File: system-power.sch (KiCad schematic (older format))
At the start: 41 parts, among them IC1 TPS63031, J1 Conn_01x02, J2 Conn_01x02, U1 MCP73831T-2ACI/OT, U2 BQ25504

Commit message: Added notes for new design
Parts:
- added C?: C, symbol Device:C
- added D?: ca. 2.2V, symbol Device:D_Zener
- added R?: 150R, symbol Device:R
- added R? (x2): 5.49M, symbol Device:R
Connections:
- net EXT_VIN: now also D?.2 (A)
- net GND: now also C?.1, R?.1, R?.2
- net VBAT_OK: now also IC1.6 (EN)
- net VBUS: now also R?.1
- net at C6.1, IC1.5 (Vin), JP2.2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: now also R?.2
- net at C7.1, IC1.7 (PS/SYNC), IC1.8 (VinA): no longer IC1.6 (EN)
- net at JP1.1, U2.14 (VBAT): now also C?.2
- new net: D?.1 (K), R?.2
- new net VSTOR: R?.1
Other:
- note added: "Dieses C ist evtl. nicht optimal\nplatziert. Mit KO vor BQ, nach BQ\nund nach DCDC-Converter Messen\nund analysieren, wo Spannung\nzusammenfällt"
- note added: "Maximum R probieren \nund dann 1-2 Werte zurück\n"
- note added: "Settings for BQ25504:\n\nVBAT_OV: 4.147 V --------\nVBAT_UV: 2.998 V\nVBAT_OK: 3.086 V\nVBAT_OK_HYST: 4.095 V\nVREF_SAMP: 0.8 V"
- note added: "Spannungsteiler für Messung\nder Batterie-Spannung. \nStimmen R?"
- note removed: "Settings for BQ25504:\n\nVBAT_OV: 4.147 V\nVBAT_UV: 2.998 V\nVBAT_OK: 3.086 V\nVBAT_OK_HYST: 4.095 V\nVREF_SAMP: 0.8 V"
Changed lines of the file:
@@
 	8350 3750 8100 3750
 Wire Wire Line
-	8100 3750 8100 3850
-Wire Wire Line
-	8350 3850 8100 3850
-Connection ~ 8100 3850
-Wire Wire Line
-	8100 3850 8100 3950
-Wire Wire Line
 	8350 3950 8100 3950
-Connection ~ 8100 3950
 Wire Wire Line
 	8350 3650 7700 3650
@@
 	2850 1650 3600 1650
 Connection ~ 3600 1650
-Text Notes 1150 3100 0    50   Italic 0
+Text Notes 500  4000 0    50   Italic 0
 For optimum voltage regulation, \nplace the battery pack as close as \npossible to the device’s VBAT and VSS pins.
 Text Notes 9800 3450 0    50   ~ 0
@@
 Connection ~ 1800 4750
 Wire Wire Line
-	1800 4750 2250 4750
+	1800 4750 2200 4750
 Wire Wire Line
 	1800 5150 1800 5200
 Wire Wire Line
 	3200 3950 3150 3950
-Wire Wire Line
-	3150 3950 3150 2850
 Wire Wire Line
 	3150 2850 3800 2850
@@
 Connection ~ 2250 4750
 Wire Wire Line
-	2250 4750 2550 4750
+	2250 4750 2200 4750
 $Comp
 L Device:LED D3
@@
 $EndComp
 Text Notes 4750 6850 0    50   ~ 0
-Settings for BQ25504:\n\nVBAT_OV: 4.147 V\nVBAT_UV: 2.998 V\nVBAT_OK: 3.086 V\nVBAT_OK_HYST: 4.095 V\nVREF_SAMP: 0.8 V
+Settings for BQ25504:\n\nVBAT_OV: 4.147 V --------\nVBAT_UV: 2.998 V\nVBAT_OK: 3.086 V\nVBAT_OK_HYST: 4.095 V\nVREF_SAMP: 0.8 V
 $Comp
 L power:PWR_FLAG #FLG02
@@
 	3600 1650 4100 1650
 Wire Wire Line
-	5750 3650 7700 3650
-Wire Wire Line
 	4500 2300 4500 2850
 Wire Wire Line
@@
 Wire Wire Line
 	2950 2550 2950 2600
-Wire Wire Line
-	2950 2600 1850 2600
 Wire Wire Line
 	1850 1450 1850 2600
@@
 Wire Wire Line
 	3100 5600 3100 5700
+Wire Wire Line
+	2200 3350 2200 4750
+Connection ~ 2200 4750
+$Comp
+L Device:C C?
+U 1 1 5F9DF573
+P 3400 3150
+F 0 "C?" V 3148 3150 50  0000 C CNN
+F 1 "C" V 3239 3150 50  0000 C CNN
+F 2 "" H 3438 3000 50  0001 C CNN
+F 3 "~" H 3400 3150 50  0001 C CNN
+	1    3400 3150
+	0    1    1    0
+$EndComp
+Wire Wire Line
+	3150 3150 3250 3150
+Connection ~ 3150 3150
+Wire Wire Line
+	3150 3150 3150 2850
+$Comp
+L power:GND #PWR?
+U 1 1 5F9E9D86
+P 3700 3200
+F 0 "#PWR?" H 3700 2950 50  0001 C CNN
+F 1 "GND" H 3705 3027 50  0000 C CNN
+F 2 "" H 3700 3200 50  0001 C CNN
+F 3 "" H 3700 3200 50  0001 C CNN
+	1    3700 3200
+	1    0    0    -1
+$EndComp
+Wire Wire Line
+	3700 3200 3700 3150
+Wire Wire Line
+	3700 3150 3550 3150
+Wire Wire Line
+	3150 3150 3150 3950
+Wire Wire Line
+	2200 2600 2200 2700
+Wire Wire Line
+	1850 2600 2200 2600
+Connection ~ 2200 2600
+Wire Wire Line
+	2200 2600 2950 2600
+Wire Wire Line
+	2250 4750 2550 4750
+$Comp
+L Device:R R?
+U 1 1 5FA4E351
+P 2200 2850
+F 0 "R?" H 2270 2896 50  0000 L CNN
+F 1 "150R" H 2270 2805 50  0000 L CNN
+F 2 "" V 2130 2850 50  0001 C CNN
+F 3 "~" H 2200 2850 50  0001 C CNN
+	1    2200 2850
+	1    0    0    -1
+$EndComp
+Wire Wire Line
+	2200 3000 2200 3050
+$Comp
+L Device:D_Zener D?
+U 1 1 5FA540F4
+P 2200 3200
+F 0 "D?" V 2154 3279 50  0000 L CNN
+F 1 "ca. 2.2V" V 2245 3279 50  0000 L CNN
+F 2 "" H 2200 3200 50  0001 C CNN
+F 3 "~" H 2200 3200 50  0001 C CNN
+	1    2200 3200
+	0    1    1    0
+$EndComp
+Text Notes 1050 3100 0    50   Italic 0
+Maximum R probieren \nund dann 1-2 Werte zurück\n
+Text GLabel 7500 4050 0    50   Input ~ 0
+VBAT_OK
+Wire Wire Line
+	7350 4050 8000 4050
+Wire Wire Line
+	8000 4050 8000 3850
+Wire Wire Line
+	8350 3850 8000 3850
+Wire Wire Line
+	8100 3750 8100 3950
+Connection ~ 8100 3950
+Text GLabel 6750 2750 1    50   Output ~ 0
+VSTOR
+Wire Wire Line
+	5750 3650 6750 3650
+$Comp
+L Device:R R?
+U 1 1 5FAAB7C8
+P 6750 3400
+F 0 "R?" H 6820 3446 50  0000 L CNN
+F 1 "5.49M" H 6820 3355 50  0000 L CNN
+F 2 "" V 6680 3400 50  0001 C CNN
+F 3 "~" H 6750 3400 50  0001 C CNN
+	1    6750 3400
+	1    0    0    -1
+$EndComp
+$Comp
+L Device:R R?
+U 1 1 5FAAEB35
+P 6750 3000
+F 0 "R?" H 6820 3046 50  0000 L CNN
+F 1 "5.49M" H 6820 2955 50  0000 L CNN
+F 2 "" V 6680 3000 50  0001 C CNN
+F 3 "~" H 6750 3000 50  0001 C CNN
+	1    6750 3000
+	1    0    0    -1
+$EndComp
+Wire Wire Line
+	6750 3250 6750 3200
+Wire Wire Line
+	6750 2850 6750 2750
+Wire Wire Line
+	6750 3650 6750 3550
+Connection ~ 6750 3650
+Wire Wire Line
+	6750 3650 7700 3650
+$Comp
+L power:GND #PWR?
+U 1 1 5FACE2D9
+P 6500 3300
+F 0 "#PWR?" H 6500 3050 50  0001 C CNN
+F 1 "GND" H 6505 3127 50  0000 C CNN
+F 2 "" H 6500 3300 50  0001 C CNN
+F 3 "" H 6500 3300 50  0001 C CNN
+	1    6500 3300
+	1    0    0    -1
+$EndComp
+Wire Wire Line
+	6500 3300 6500 3200
+Wire Wire Line
+	6500 3200 6750 3200
+Connection ~ 6750 3200
+Wire Wire Line
+	6750 3200 6750 3150
+Text Notes 5550 3050 0    50   Italic 0
+Spannungsteiler für Messung\nder Batterie-Spannung. \nStimmen R?
+Text Notes 3750 3300 0    50   Italic 0
+Dieses C ist evtl. nicht optimal\nplatziert. Mit KO vor BQ, nach BQ\nund nach DCDC-Converter Messen\nund analysieren, wo Spannung\nzusammenfällt
 $EndSCHEMATC

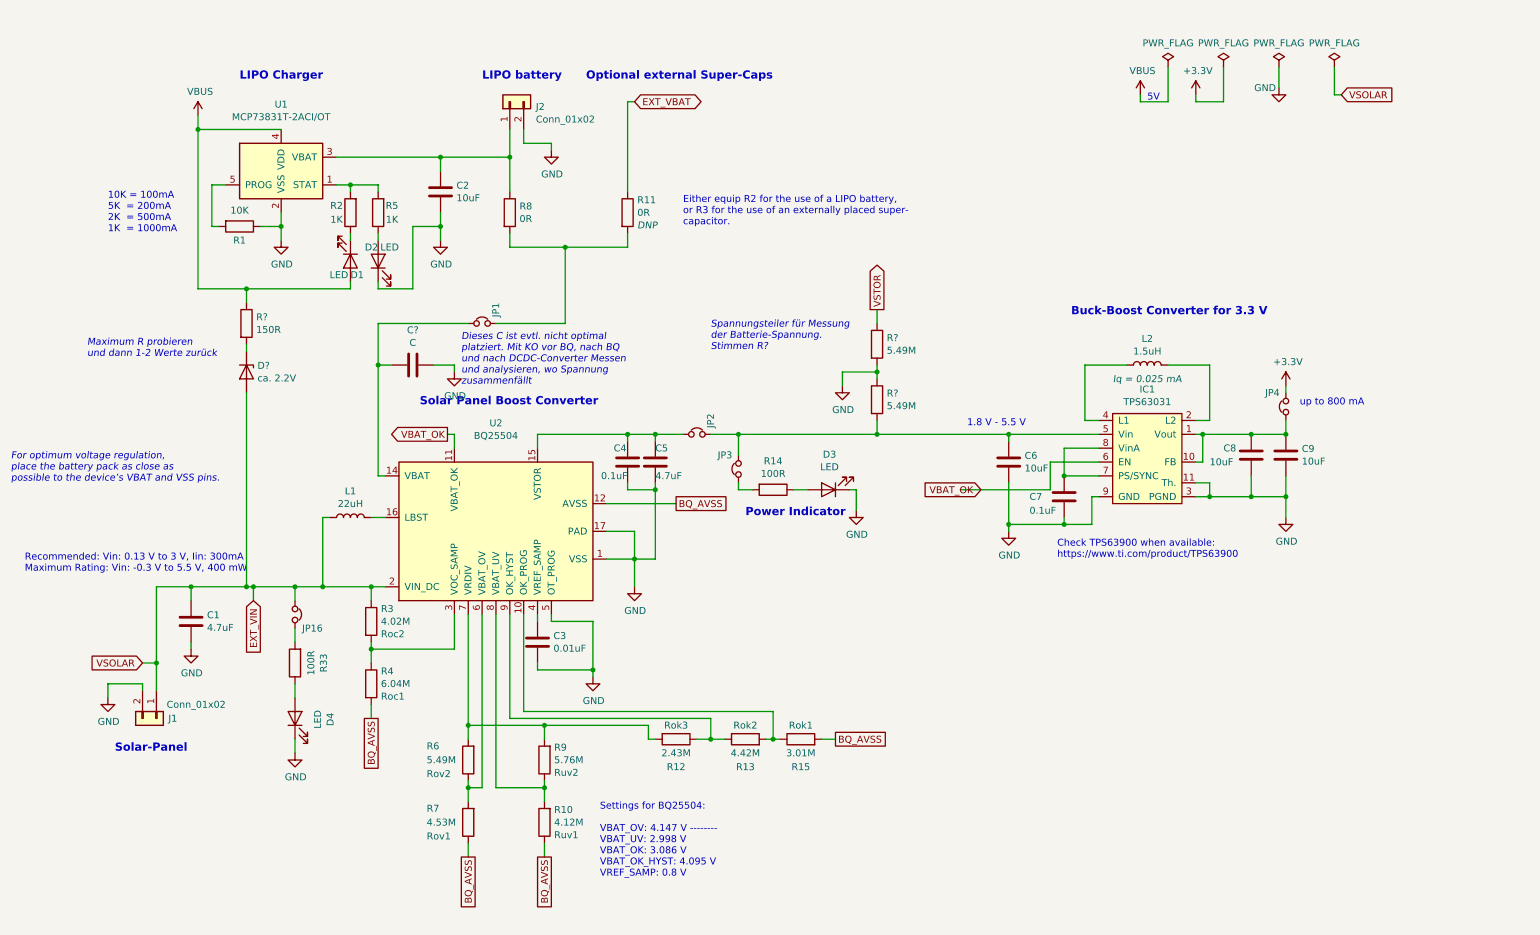
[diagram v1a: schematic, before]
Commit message: Fixed issue #2, #3, #4 and #5
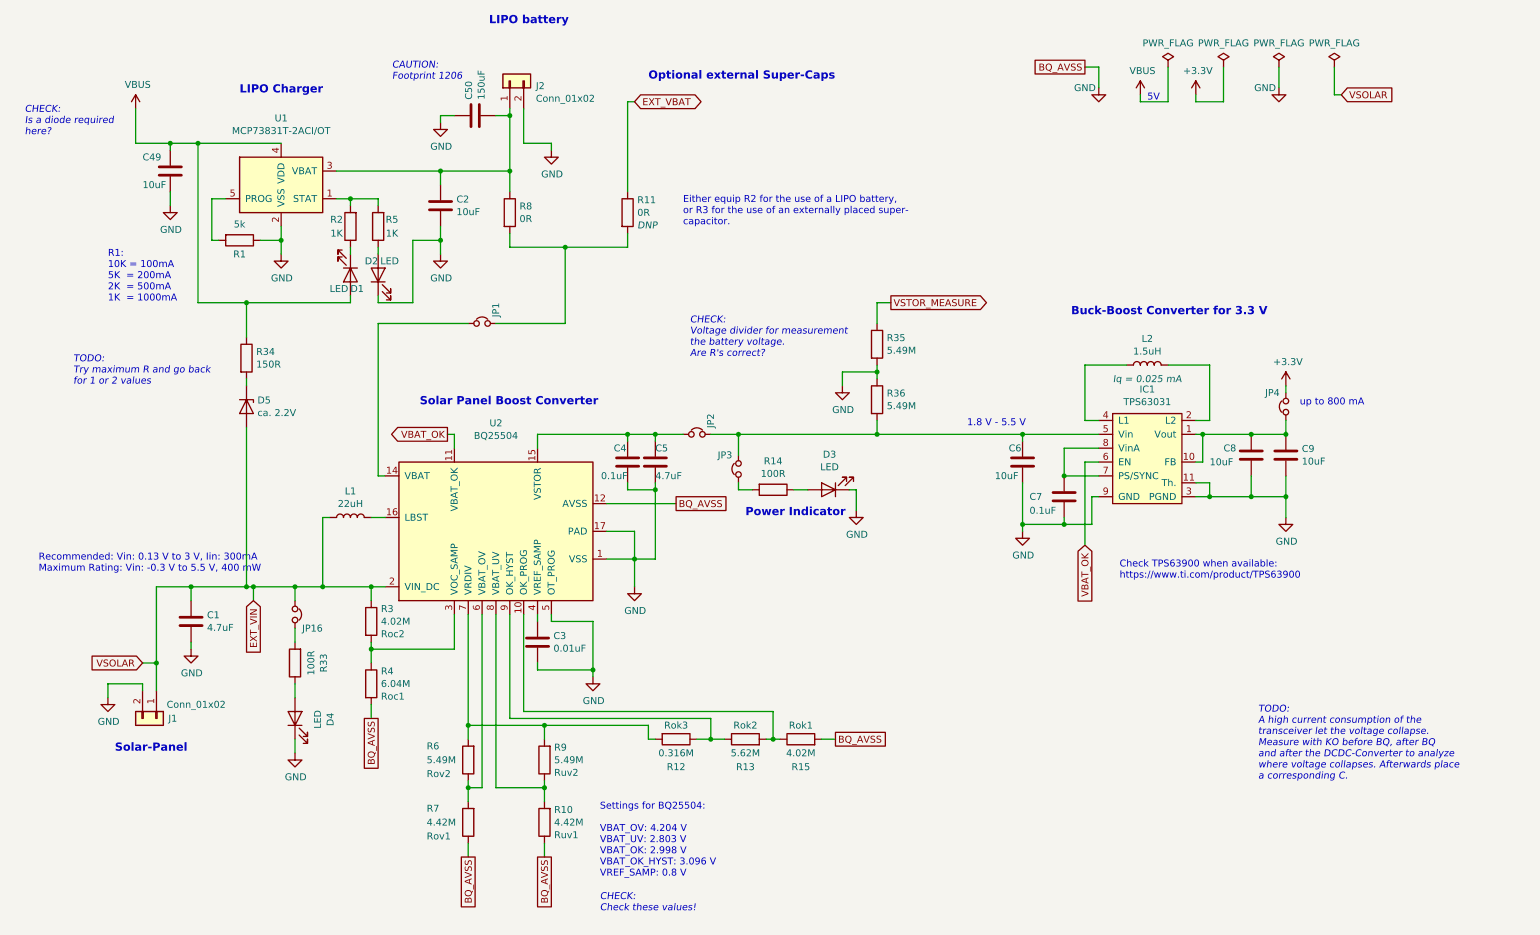
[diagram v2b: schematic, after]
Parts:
- removed C?: C, symbol Device:C
- added C49: 10uF, Capacitor_SMD:C_0402_1005Metric, symbol Device:C
- added C50: 150uF, Capacitor_SMD:C_0402_1005Metric, symbol Device:C
- R1: value 10K -> 5k
- R10: value 4.12M -> 4.42M
- R12: value 2.43M -> 0.316M
- R13: value 4.42M -> 5.62M
- R15: value 3.01M -> 4.02M
- R7: value 4.53M -> 4.42M
- R9: value 5.76M -> 5.49M
- gave numbers to parts that had none: 4
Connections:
- net BQ_AVSS is gone; now on net GND: R10.1, R15.2, R4.2, R7.1, U2.12 (AVSS)
- net GND: now also C49.2, C50.1
- net VBUS: now also C49.1
- net at C2.1, J2.1 (Pin_1), R8.1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: now also C50.2
- net VSTOR renamed VSTOR_MEASURE
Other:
- note added: "CAUTION:\nFootprint 1206"
- note added: "CHECK:\nCheck these values!"
- note added: "CHECK:\nIs a diode required \nhere?"
- note added: "CHECK:\nVoltage divider for measurement\nthe battery voltage. \nAre R's correct?"
- note added: "R1:\n10K = 100mA\n5K = 200mA\n2K = 500mA\n1K = 1000mA"
- note added: "Settings for BQ25504:\n\nVBAT_OV: 4.204 V\nVBAT_UV: 2.803 V\nVBAT_OK: 2.998 V\nVBAT_OK_HYST: 3.096 V\nVREF_SAMP: 0.8 V"
- note added: "TODO:\nA high current consumption of the\ntransceiver let the voltage collapse.\nMeasure with KO before BQ, after BQ\nand after the DCDC-Converter to analyze \nwhere voltage collapses. Afterwards place\na corresponding C."
- note added: "TODO:\nTry maximum R and go back\nfor 1 or 2 values"
- note removed: "10K = 100mA\n5K = 200mA\n2K = 500mA\n1K = 1000mA"
- note removed: "Dieses C ist evtl. nicht optimal\nplatziert. Mit KO vor BQ, nach BQ\nund nach DCDC-Converter Messen\nund analysieren, wo Spannung\nzusammenfällt"
- note removed: "For optimum voltage regulation, \nplace the battery pack as close as \npossible to the device’s VBAT and VSS pins."
- note removed: "Maximum R probieren \nund dann 1-2 Werte zurück\n"
- note removed: "Settings for BQ25504:\n\nVBAT_OV: 4.147 V --------\nVBAT_UV: 2.998 V\nVBAT_OK: 3.086 V\nVBAT_OK_HYST: 4.095 V\nVREF_SAMP: 0.8 V"
- note removed: "Spannungsteiler für Messung\nder Batterie-Spannung. \nStimmen R?"
- moved on the sheet: C2, C6, D1, D2, D5, J2, R1, R2, R34, R5, U1

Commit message: Removed unnecessary leds from system-power to save power
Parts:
- removed D3, D4: LED, LED_SMD:LED_0603_1608Metric, symbol Device:LED
- removed JP16, JP3: Jumper_NC_Small, Connector_PinHeader_2.54mm:PinHeader_1x02_P2.54mm_Vertical, symbol Device:Jumper_NC_Small
- removed R14, R33: 100R, Resistor_SMD:R_0402_1005Metric, symbol Device:R
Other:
- note removed: "Power Indicator"

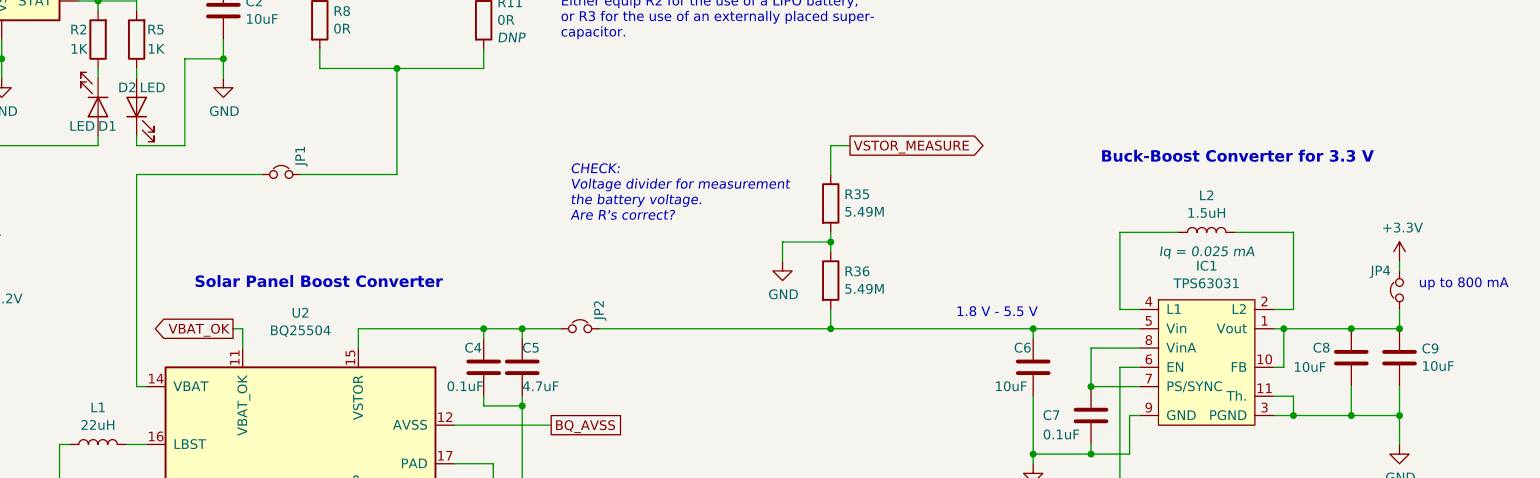
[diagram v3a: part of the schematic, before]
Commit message: Removed jumpers from system-power
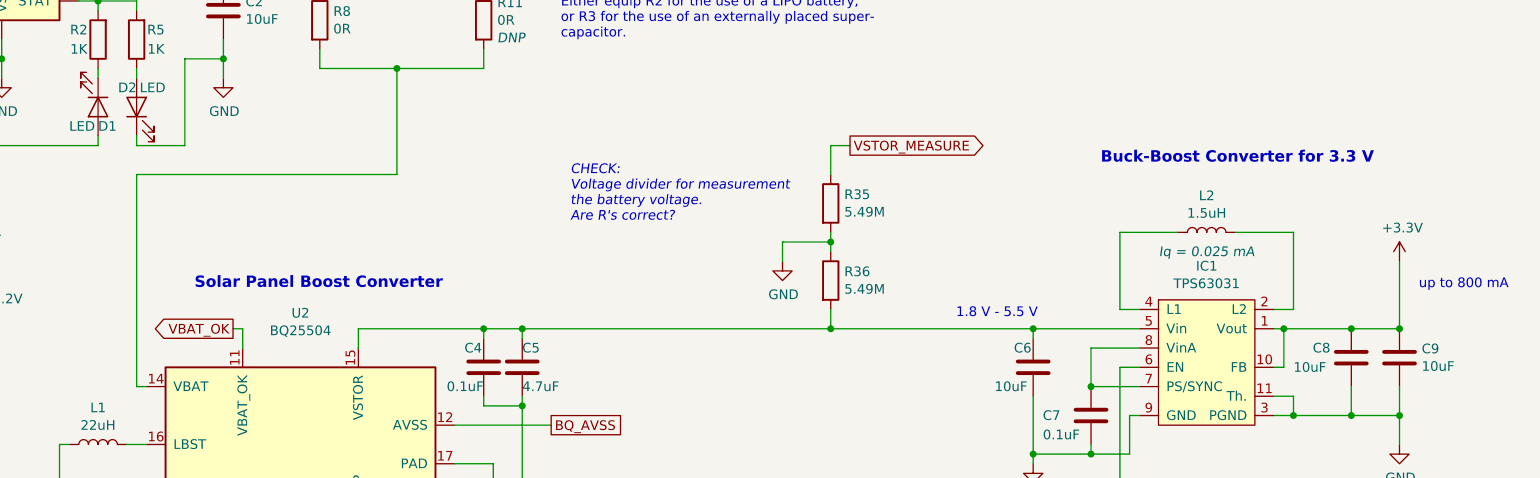
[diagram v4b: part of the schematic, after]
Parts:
- removed JP1, JP2, JP4: Jumper_NC_Small, Connector_PinHeader_2.54mm:PinHeader_1x02_P2.54mm_Vertical, symbol Device:Jumper_NC_Small
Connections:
- net +3V3: now also C8.1, C9.1, IC1.1 (Vout), IC1.10 (FB)
- net at R11.2, R8.2: now also U2.14 (VBAT)
- net at C6.1, IC1.5 (Vin), R36.2: now also C4.1, C5.1, U2.15 (VSTOR)
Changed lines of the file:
@@
 $EndComp
-Wire Wire Line
-	9700 3300 9700 3350
 Wire Wire Line
 	9700 3950 9700 4100
@@
 Wire Wire Line
 	4350 5750 5100 5750
-Wire Wire Line
-	5150 3650 5350 3650
 $Comp
 L Device:R R3
@@
 Text Notes 8150 2800 0    59   ~ 12
 Buck-Boost Converter for 3.3 V
-$Comp
-L Device:Jumper_NC_Small JP?
-U 1 1 5FB4A073
-P 9700 3450
-AR Path="/5F6D82DD/5FB4A073" Ref="JP?"  Part="1"
-AR Path="/5F687AA1/5FB4A073" Ref="JP4"  Part="1"
-F 0 "JP4" V 9800 3600 50  0000 R CNN
-F 1 "Jumper_NC_Small" V 9655 3403 50  0001 R CNN
-F 2 "Connector_PinHeader_2.54mm:PinHeader_1x02_P2.54mm_Vertical" H 9700 3450 50  0001 C CNN
-F 3 "~" H 9700 3450 50  0001 C CNN
-	1    9700 3450
-	0    -1   -1   0
-$EndComp
-Wire Wire Line
-	9700 3550 9700 3650
-$Comp
-L Device:Jumper_NC_Small JP?
-U 1 1 5FB63904
-P 5450 3650
-AR Path="/5F6D82DD/5FB63904" Ref="JP?"  Part="1"
-AR Path="/5F687AA1/5FB63904" Ref="JP2"  Part="1"
-F 0 "JP2" V 5550 3800 50  0000 R CNN
-F 1 "Jumper_NC_Small" V 5405 3603 50  0001 R CNN
-F 2 "Connector_PinHeader_2.54mm:PinHeader_1x02_P2.54mm_Vertical" H 5450 3650 50  0001 C CNN
-F 3 "~" H 5450 3650 50  0001 C CNN
-	1    5450 3650
-	1    0    0    -1
-$EndComp
 Text GLabel 3650 3650 0    50   Output ~ 0
 VBAT_OK
@@
 CAUTION:\nFootprint 1206
 Wire Wire Line
-	4000 2850 4500 2850
-Wire Wire Line
-	3150 2850 3800 2850
-$Comp
-L Device:Jumper_NC_Small JP?
-U 1 1 5FB646D7
-P 3900 2850
-AR Path="/5F6D82DD/5FB646D7" Ref="JP?"  Part="1"
-AR Path="/5F687AA1/5FB646D7" Ref="JP1"  Part="1"
-F 0 "JP1" V 4000 3000 50  0000 R CNN
-F 1 "Jumper_NC_Small" V 3855 2803 50  0001 R CNN
-F 2 "Connector_PinHeader_2.54mm:PinHeader_1x02_P2.54mm_Vertical" H 3900 2850 50  0001 C CNN
-F 3 "~" H 3900 2850 50  0001 C CNN
-	1    3900 2850
-	1    0    0    -1
-$EndComp
-Wire Wire Line
 	2250 4750 2750 4750
 Wire Wire Line
-	5550 3650 6750 3650
+	3150 2850 4500 2850
+Wire Wire Line
+	5150 3650 6750 3650
+Wire Wire Line
+	9700 3300 9700 3650
 $EndSCHEMATC

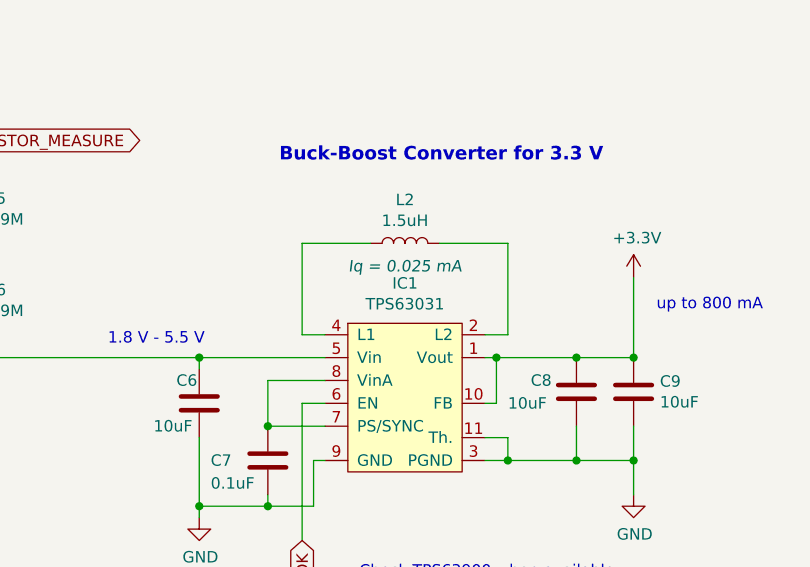
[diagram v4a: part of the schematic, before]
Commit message: Changed all symbols names from IC to U
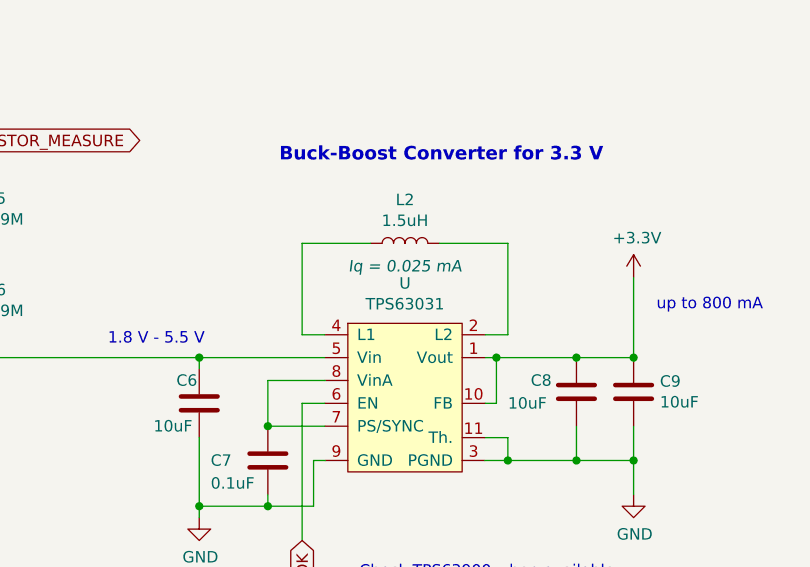
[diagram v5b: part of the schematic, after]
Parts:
- renumbered IC1 to U
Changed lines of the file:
@@
 $EndComp
 $Comp
-L tardigrade-components:TPS63031 IC1
+L tardigrade-components:TPS63031 U
 U 1 1 5F6C19C3
 P 8700 3850
-F 0 "IC1" H 8700 4375 50  0000 C CNN
+F 0 "U" H 8700 4375 50  0000 C CNN
 F 1 "TPS63031" H 8700 4284 50  0000 C CNN
 F 2 "tardigrade-components:TPS63031DSKR" H 8700 4050 50  0001 C CNN
